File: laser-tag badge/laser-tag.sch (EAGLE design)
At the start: 34 parts, among them U1 MKL27Z256VLH4

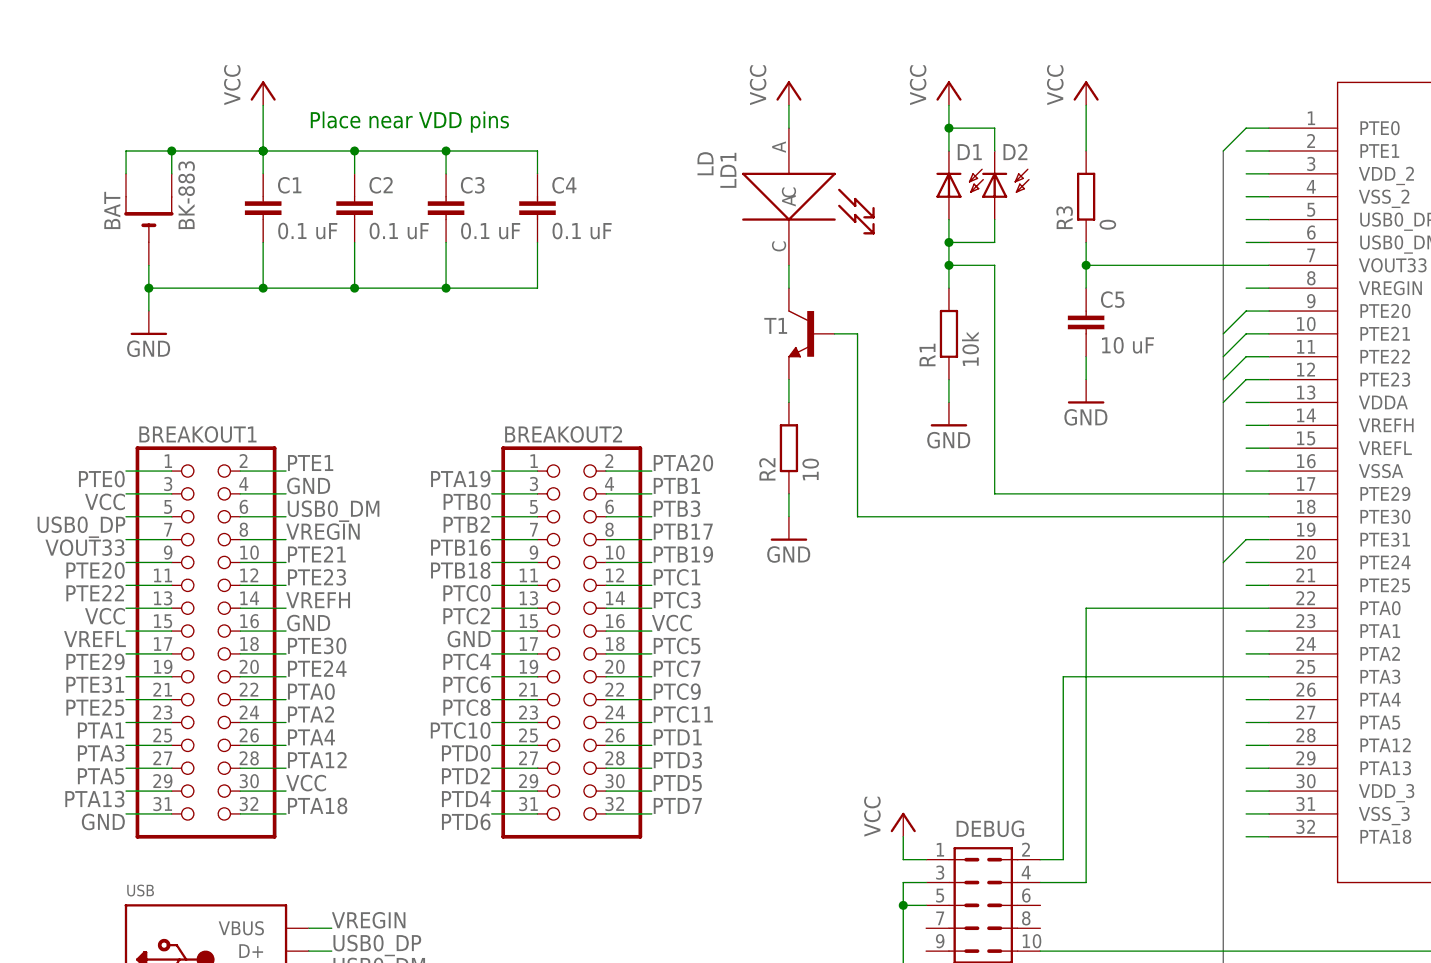
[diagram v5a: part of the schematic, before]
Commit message: Fix transistor, tie VREFL low, add WS2812B
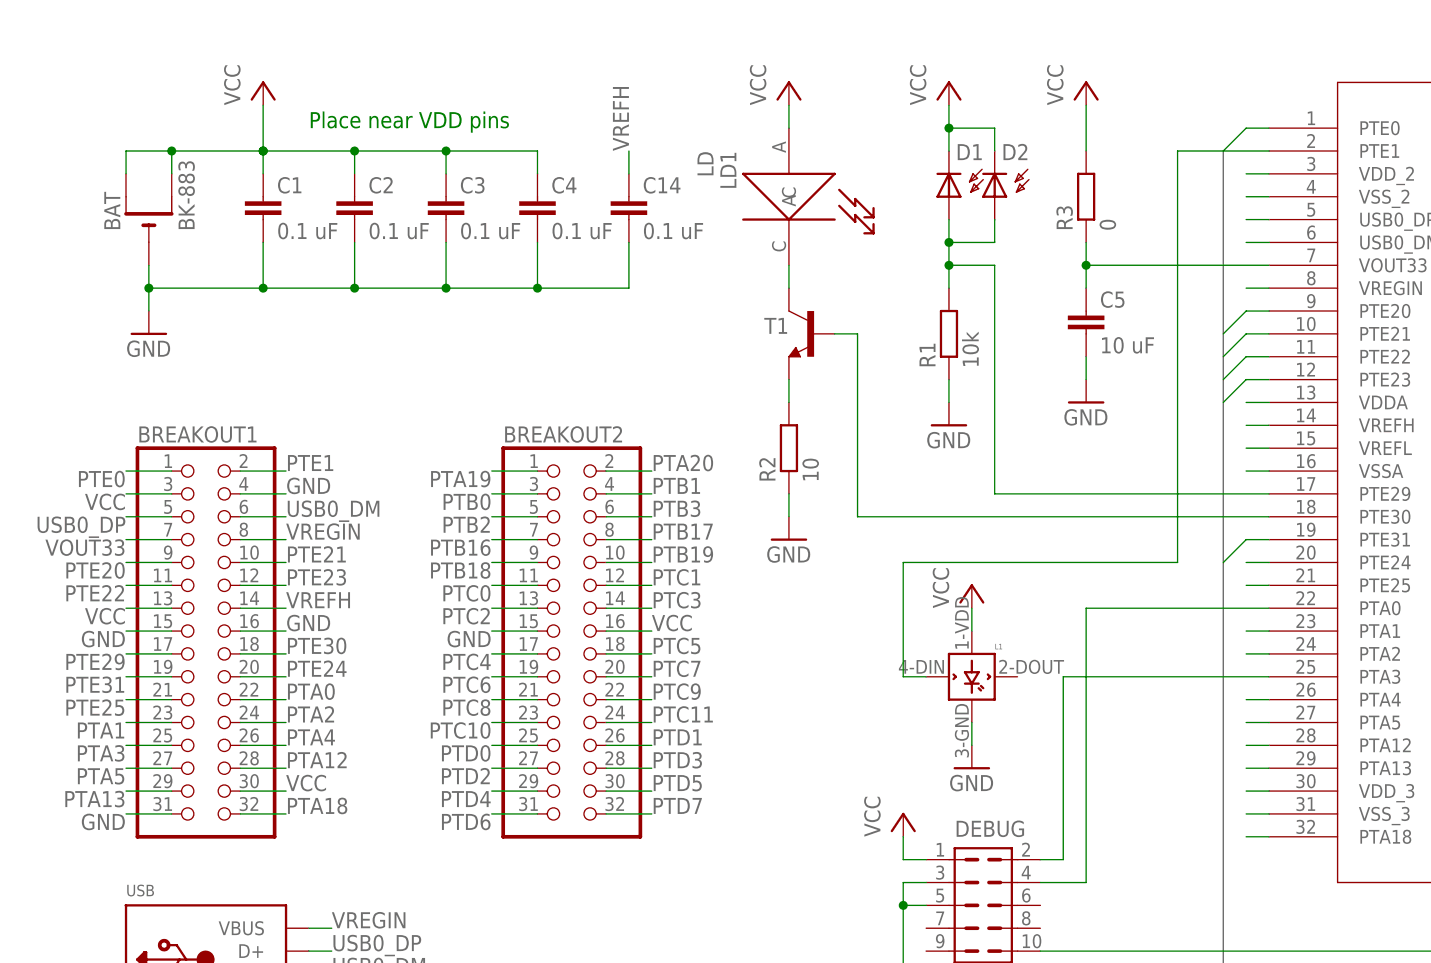
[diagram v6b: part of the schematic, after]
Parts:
- added C14: 0.1 uF, rcl:C-EUC0603K
- added L1: WS2812B, adafruit:WS2812B
- T1, T2: device transistor:-NPN-SOT23-EBC -> transistor:BC850-NPN-SOT23-BEC
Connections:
- removed net VREFL: BREAKOUT1.15, U1.VREFL
- net GND: now also BREAKOUT1.15, C14.2, L1.GND, U1.VREFL
- net PTE1: now also L1.DIN
- net VCC: now also L1.VDD
- net VREFH: now also C14.1
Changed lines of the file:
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@@
 <part name="LD1" library="Photonics" deviceset="LD" device=""/>
 <part name="P+1" library="supply1" deviceset="VCC" device=""/>
-<part name="T1" library="transistor" deviceset="*-NPN-" device="SOT23-EBC"/>
+<part name="T1" library="transistor" deviceset="*-NPN-" device="SOT23-BEC" technology="BC850"/>
 <part name="GND1" library="supply1" deviceset="GND" device=""/>
 <part name="P+2" library="supply1" deviceset="VCC" device=""/>
@@
 <part name="GND6" library="supply1" deviceset="GND" device=""/>
 <part name="GND7" library="supply1" deviceset="GND" device=""/>
-<part name="T2" library="transistor" deviceset="*-NPN-" device="SOT23-EBC"/>
+<part name="T2" library="transistor" deviceset="*-NPN-" device="SOT23-BEC" technology="BC850"/>
 <part name="R4" library="rcl" deviceset="R-EU_" device="R0603" value="10"/>
 <part name="P+7" library="supply1" deviceset="VCC" device=""/>
@@
 <part name="D2" library="Photonics" deviceset="PDB-C154SM" device=""/>
 <part name="U$1" library="Graphics" deviceset="AHA" device=""/>
+<part name="L1" library="adafruit" deviceset="WS2812B" device=""/>
+<part name="P+6" library="supply1" deviceset="VCC" device=""/>
+<part name="GND9" library="supply1" deviceset="GND" device=""/>
+<part name="C14" library="rcl" deviceset="C-EU" device="C0603K" value="0.1 uF"/>
 </parts>
 <sheets>
@@
 </instance>
 <instance part="U$1" gate="G$1" x="-66.04" y="-10.16"/>
+<instance part="L1" gate="G$1" x="-22.86" y="38.1"/>
+<instance part="P+6" gate="VCC" x="-22.86" y="48.26"/>
+<instance part="GND9" gate="1" x="-22.86" y="27.94"/>
+<instance part="C14" gate="G$1" x="-60.96" y="91.44"/>
 </instances>
 <busses>
@@
 <wire x1="-71.12" y1="81.28" x2="-71.12" y2="86.36" width="0.1524" layer="91"/>
 <junction x="-81.28" y="81.28"/>
+<pinref part="C14" gate="G$1" pin="2"/>
+<wire x1="-71.12" y1="81.28" x2="-60.96" y2="81.28" width="0.1524" layer="91"/>
+<wire x1="-60.96" y1="81.28" x2="-60.96" y2="86.36" width="0.1524" layer="91"/>
+<junction x="-71.12" y="81.28"/>
 </segment>
 <segment>
@@
 <junction x="157.48" y="27.94"/>
 </segment>
+<segment>
+<pinref part="GND9" gate="1" pin="GND"/>
+<pinref part="L1" gate="G$1" pin="GND"/>
+<wire x1="-22.86" y1="30.48" x2="-22.86" y2="33.02" width="0.1524" layer="91"/>
+</segment>
+<segment>
+<pinref part="U1" gate="A" pin="VREFL"/>
+<wire x1="10.16" y1="63.5" x2="7.62" y2="63.5" width="0.1524" layer="91"/>
+</segment>
+<segment>
+<pinref part="BREAKOUT1" gate="A" pin="15"/>
+<wire x1="-111.76" y1="43.18" x2="-116.84" y2="43.18" width="0.1524" layer="91"/>
+<label x="-116.84" y="43.18" size="1.778" layer="95" rot="R180"/>
+</segment>
 </net>
 <net name="VCC" class="0">
@@
 <junction x="10.16" y="-7.62"/>
 </segment>
+<segment>
+<pinref part="P+6" gate="VCC" pin="VCC"/>
+<pinref part="L1" gate="G$1" pin="VDD"/>
+<wire x1="-22.86" y1="45.72" x2="-22.86" y2="43.18" width="0.1524" layer="91"/>
+</segment>
 </net>
 <net name="PTA3" class="0">
@@
 <segment>
 <pinref part="U1" gate="A" pin="PTE1"/>
-<wire x1="10.16" y1="96.52" x2="7.62" y2="96.52" width="0.1524" layer="91"/>
+<wire x1="10.16" y1="96.52" x2="0" y2="96.52" width="0.1524" layer="91"/>
+<wire x1="0" y1="96.52" x2="0" y2="50.8" width="0.1524" layer="91"/>
+<wire x1="0" y1="50.8" x2="-30.48" y2="50.8" width="0.1524" layer="91"/>
+<wire x1="-30.48" y1="50.8" x2="-30.48" y2="38.1" width="0.1524" layer="91"/>
+<pinref part="L1" gate="G$1" pin="DIN"/>
+<wire x1="-30.48" y1="38.1" x2="-27.94" y2="38.1" width="0.1524" layer="91"/>
 </segment>
 </net>
@@
 <label x="-99.06" y="45.72" size="1.778" layer="95"/>
 </segment>
-</net>
-<net name="VREFL" class="0">
-<segment>
-<pinref part="U1" gate="A" pin="VREFL"/>
-<wire x1="10.16" y1="63.5" x2="7.62" y2="63.5" width="0.1524" layer="91"/>
-</segment>
-<segment>
-<pinref part="BREAKOUT1" gate="A" pin="15"/>
-<wire x1="-111.76" y1="43.18" x2="-116.84" y2="43.18" width="0.1524" layer="91"/>
-<label x="-116.84" y="43.18" size="1.778" layer="95" rot="R180"/>
-</segment>
-</net>
+<segment>
+<pinref part="C14" gate="G$1" pin="1"/>
+<wire x1="-60.96" y1="93.98" x2="-60.96" y2="96.52" width="0.1524" layer="91"/>
+<label x="-60.96" y="96.52" size="1.778" layer="95" rot="R90"/>
+</segment>
+</net>

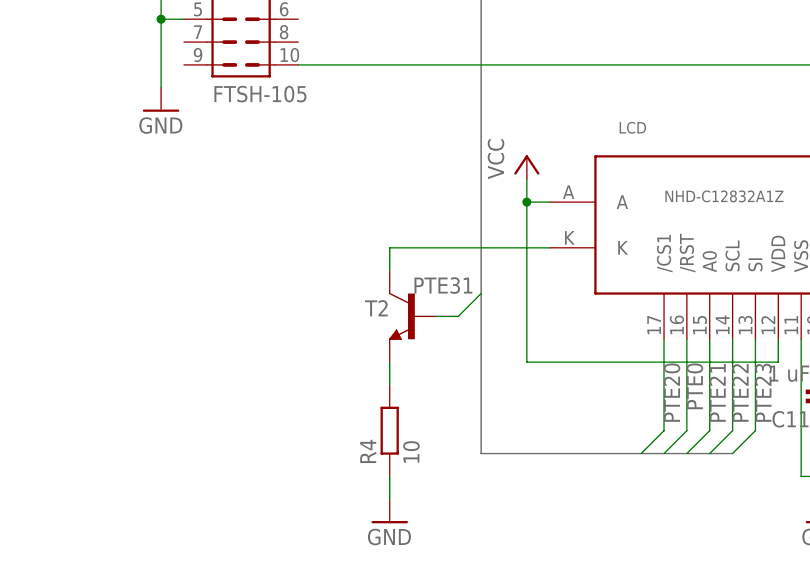
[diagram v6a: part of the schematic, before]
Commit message: Fix backlight LED circuit
Use a FET instead of a BJT since we're just switching it on and off
and don't want to draw a lot of current from the MCU.
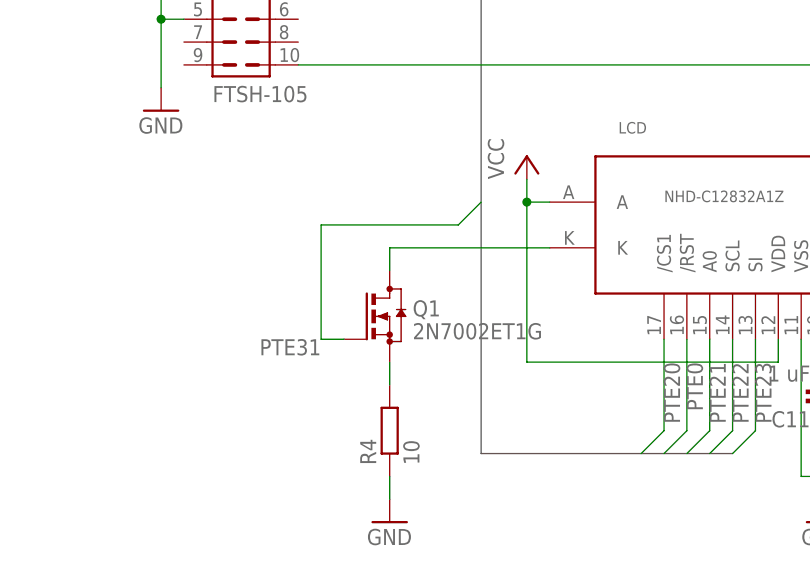
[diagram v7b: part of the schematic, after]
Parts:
- removed T2: (no value), transistor:BC850-NPN-SOT23-BEC
- added Q1: 2N7002ET1G, transistor-small-signal:BSS123
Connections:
- net N$13: now also Q1.D; no longer T2.C
- net N$14: now also Q1.S; no longer T2.E
- net PTE31: now also Q1.G; no longer T2.B
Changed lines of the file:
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@@
 <part name="GND6" library="supply1" deviceset="GND" device=""/>
 <part name="GND7" library="supply1" deviceset="GND" device=""/>
-<part name="T2" library="transistor" deviceset="*-NPN-" device="SOT23-BEC" technology="BC850"/>
 <part name="R4" library="rcl" deviceset="R-EU_" device="R0603" value="10"/>
 <part name="P+7" library="supply1" deviceset="VCC" device=""/>
@@
 <part name="GND9" library="supply1" deviceset="GND" device=""/>
 <part name="C14" library="rcl" deviceset="C-EU" device="C0603K" value="0.1 uF"/>
+<part name="Q1" library="transistor-small-signal" deviceset="BSS123" device="" value="2N7002ET1G"/>
 </parts>
 <sheets>
@@
 <instance part="GND6" gate="1" x="43.18" y="-43.18"/>
 <instance part="GND7" gate="1" x="-5.08" y="-43.18"/>
-<instance part="T2" gate="G$1" x="-2.54" y="-20.32" smashed="yes" rot="MR0">
-<attribute name="NAME" x="-5.08" y="-20.32" size="1.778" layer="95" rot="MR0"/>
-<attribute name="VALUE" x="7.62" y="-15.24" size="1.778" layer="96" rot="MR0"/>
-</instance>
 <instance part="R4" gate="G$1" x="-5.08" y="-33.02" rot="R90"/>
 <instance part="P+7" gate="VCC" x="10.16" y="-2.54"/>
@@
 <instance part="GND9" gate="1" x="-22.86" y="27.94"/>
 <instance part="C14" gate="G$1" x="-60.96" y="91.44"/>
+<instance part="Q1" gate="G$1" x="-5.08" y="-20.32"/>
 </instances>
 <busses>
@@
 </segment>
 <segment>
-<pinref part="T2" gate="G$1" pin="B"/>
-<wire x1="0" y1="-20.32" x2="2.54" y2="-20.32" width="0.1524" layer="91"/>
-<label x="-2.54" y="-17.78" size="1.778" layer="95"/>
-<wire x1="2.54" y1="-20.32" x2="5.08" y2="-17.78" width="0.1524" layer="91"/>
+<wire x1="-12.7" y1="-10.16" x2="2.54" y2="-10.16" width="0.1524" layer="91"/>
+<label x="-12.7" y="-22.86" size="1.778" layer="95" rot="R180"/>
+<wire x1="2.54" y1="-10.16" x2="5.08" y2="-7.62" width="0.1524" layer="91"/>
+<wire x1="-12.7" y1="-10.16" x2="-12.7" y2="-22.86" width="0.1524" layer="91"/>
+<pinref part="Q1" gate="G$1" pin="G"/>
+<wire x1="-12.7" y1="-22.86" x2="-10.16" y2="-22.86" width="0.1524" layer="91"/>
 </segment>
 </net>
@@
 <segment>
 <pinref part="LCD" gate="G$1" pin="K"/>
-<pinref part="T2" gate="G$1" pin="C"/>
 <wire x1="12.7" y1="-12.7" x2="-5.08" y2="-12.7" width="0.1524" layer="91"/>
 <wire x1="-5.08" y1="-12.7" x2="-5.08" y2="-15.24" width="0.1524" layer="91"/>
+<pinref part="Q1" gate="G$1" pin="D"/>
 </segment>
 </net>
 <net name="N$14" class="0">
 <segment>
-<pinref part="T2" gate="G$1" pin="E"/>
 <pinref part="R4" gate="G$1" pin="2"/>
 <wire x1="-5.08" y1="-25.4" x2="-5.08" y2="-27.94" width="0.1524" layer="91"/>
-</segment>
-</net>
+<pinref part="Q1" gate="G$1" pin="S"/>
+</segment>
+</net>
